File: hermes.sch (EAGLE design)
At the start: 13 parts

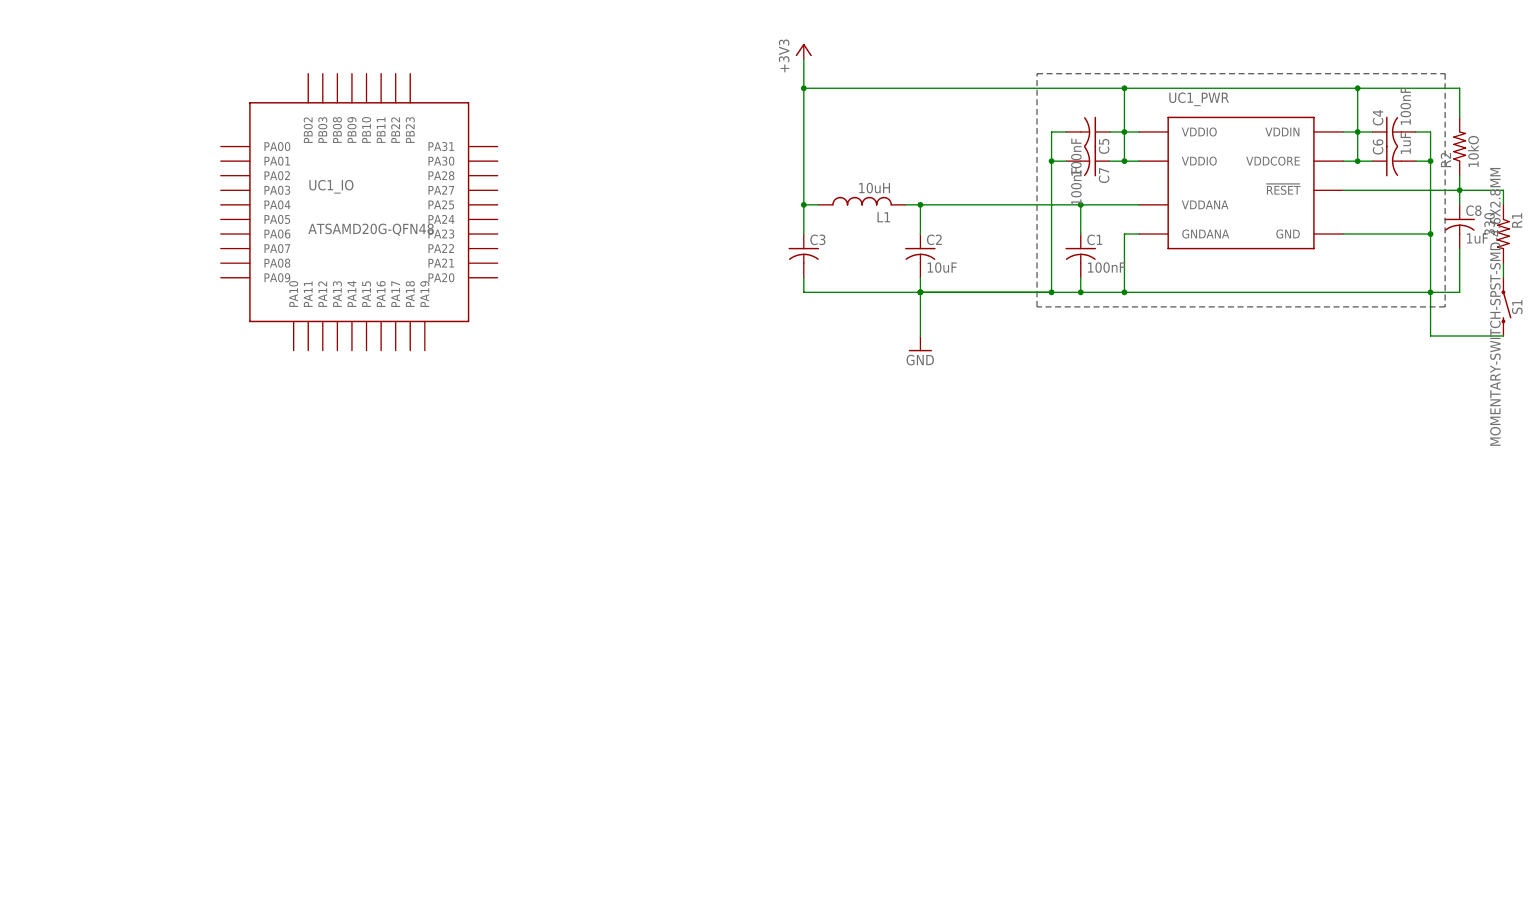
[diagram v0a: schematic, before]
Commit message: -Add LDO -Add library -Notes to uC PWR
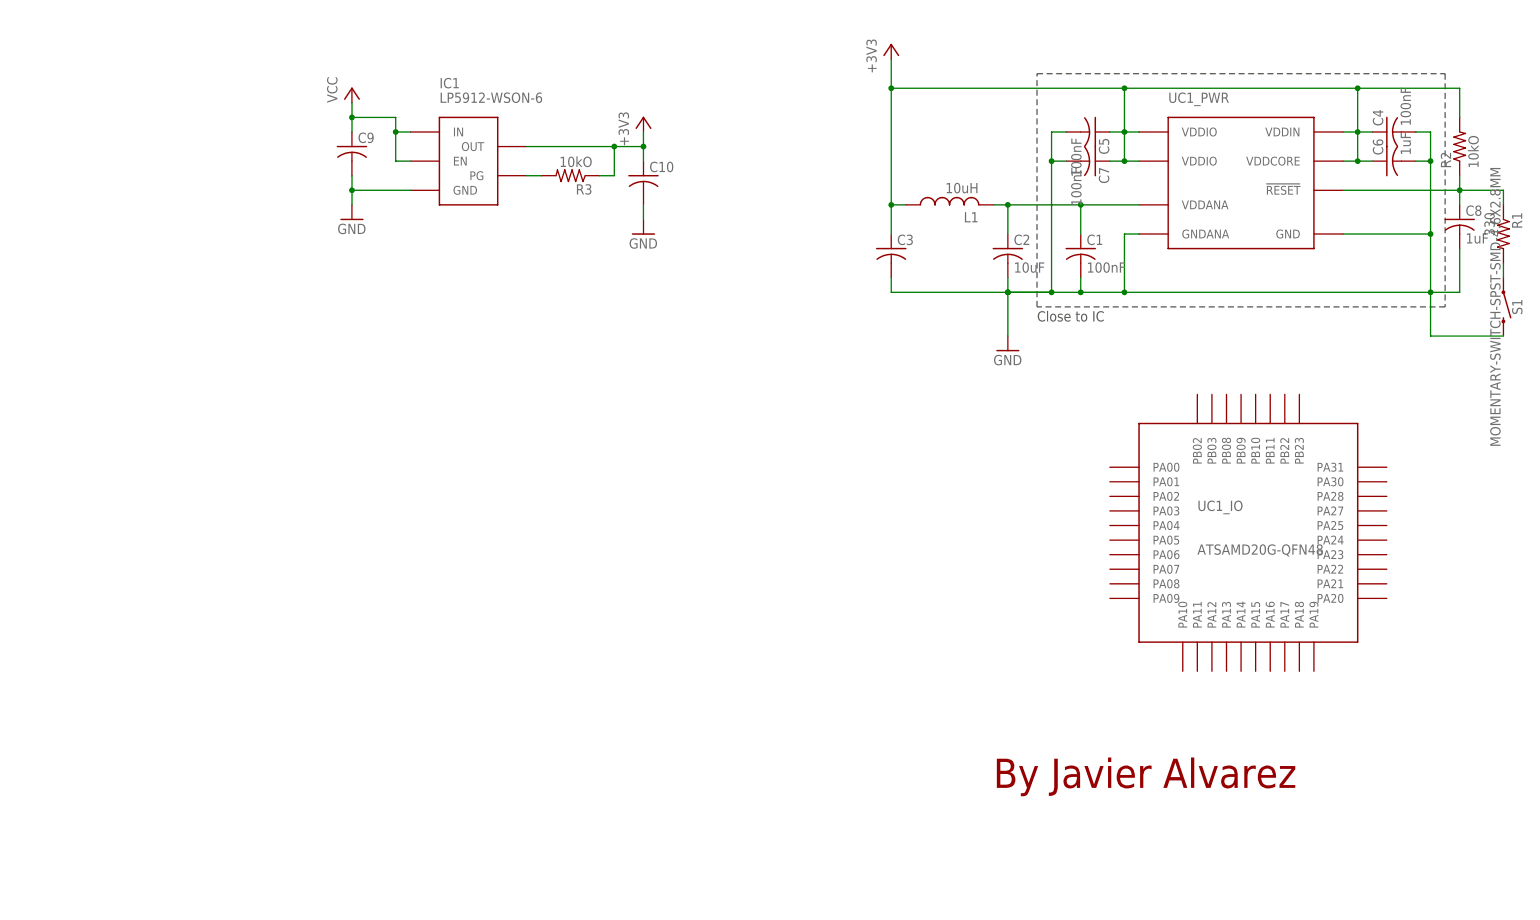
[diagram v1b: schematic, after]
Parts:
- added C10, C9: (no value), rcl:C-USC0201
- added IC1: LP5912-WSON-6, Hermes_lib:LP5912-WSON-6
- added R3: 10kO, rcl:R-US_R0201
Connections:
- new net N$4: IC1.PG, R3.2
- new net VCC: C9.1, IC1.EN, IC1.IN
- net +3V3: now also C10.1, IC1.OUT, R3.1
- net GND: now also C10.2, C9.2, IC1.GND
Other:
- note added: "By Javier Alvarez"
- note added: "Close to IC"
- moved on the sheet: C2, C3, L1, UC1_IO
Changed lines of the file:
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@@
 <part name="C8" library="rcl" library_urn="urn:adsk.eagle:library:334" deviceset="C-US" device="C0201" package3d_urn="urn:adsk.eagle:package:23690/1" value="1uF"/>
 <part name="S1" library="SparkFun-Switches" library_urn="urn:adsk.eagle:library:535" deviceset="MOMENTARY-SWITCH-SPST" device="-SMD-4.6X2.8MM" package3d_urn="urn:adsk.eagle:package:40176/1"/>
+<part name="IC1" library="Hermes_lib" library_urn="urn:adsk.eagle:library:1022648" deviceset="LP5912-" device="WSON-6" package3d_urn="urn:adsk.eagle:package:1286349/1"/>
+<part name="C9" library="rcl" library_urn="urn:adsk.eagle:library:334" deviceset="C-US" device="C0201" package3d_urn="urn:adsk.eagle:package:23690/1"/>
+<part name="R3" library="rcl" library_urn="urn:adsk.eagle:library:334" deviceset="R-US_" device="R0201" package3d_urn="urn:adsk.eagle:package:23593/1" value="10kO"/>
+<part name="C10" library="rcl" library_urn="urn:adsk.eagle:library:334" deviceset="C-US" device="C0201" package3d_urn="urn:adsk.eagle:package:23690/1"/>
+<part name="P+1" library="supply1" library_urn="urn:adsk.eagle:library:371" deviceset="VCC" device=""/>
+<part name="GND2" library="supply1" library_urn="urn:adsk.eagle:library:371" deviceset="GND" device=""/>
+<part name="GND3" library="supply1" library_urn="urn:adsk.eagle:library:371" deviceset="GND" device=""/>
+<part name="+3V2" library="supply1" library_urn="urn:adsk.eagle:library:371" deviceset="+3V3" device=""/>
 </parts>
 <sheets>
@@
 <wire x1="246.38" y1="111.76" x2="175.26" y2="111.76" width="0.1524" layer="97" style="shortdash"/>
 <wire x1="175.26" y1="111.76" x2="175.26" y2="152.4" width="0.1524" layer="97" style="shortdash"/>
+<text x="175.26" y="109.22" size="1.778" layer="97">Close to IC</text>
+<text x="167.64" y="27.94" size="5.08" layer="94">By Javier Alvarez</text>
 </plain>
 <instances>
 <instance part="FRAME1" gate="G$1" x="0" y="0"/>
 <instance part="FRAME1" gate="G$2" x="162.56" y="0"/>
-<instance part="UC1" gate="_IO" x="58.42" y="129.54"/>
+<instance part="UC1" gate="_IO" x="213.36" y="73.66"/>
 <instance part="UC1" gate="_PWR" x="210.82" y="134.62"/>
-<instance part="+3V1" gate="G$1" x="134.62" y="157.48"/>
-<instance part="GND1" gate="1" x="154.94" y="104.14"/>
-<instance part="L1" gate="G$1" x="144.78" y="129.54" rot="R90"/>
+<instance part="+3V1" gate="G$1" x="149.86" y="157.48"/>
+<instance part="GND1" gate="1" x="170.18" y="104.14"/>
+<instance part="L1" gate="G$1" x="160.02" y="129.54" rot="R90"/>
 <instance part="C1" gate="G$1" x="182.88" y="121.92"/>
-<instance part="C2" gate="G$1" x="154.94" y="121.92"/>
-<instance part="C3" gate="G$1" x="134.62" y="121.92"/>
+<instance part="C2" gate="G$1" x="170.18" y="121.92"/>
+<instance part="C3" gate="G$1" x="149.86" y="121.92"/>
 <instance part="C4" gate="G$1" x="236.22" y="142.24" rot="R90"/>
 <instance part="C5" gate="G$1" x="185.42" y="142.24" rot="R270"/>
@@
 <instance part="C8" gate="G$1" x="248.92" y="127"/>
 <instance part="S1" gate="G$1" x="256.54" y="111.76" rot="R270"/>
+<instance part="IC1" gate="G$1" x="73.66" y="134.62"/>
+<instance part="C9" gate="G$1" x="55.88" y="139.7"/>
+<instance part="R3" gate="G$1" x="93.98" y="134.62" rot="R180"/>
+<instance part="C10" gate="G$1" x="106.68" y="134.62"/>
+<instance part="P+1" gate="VCC" x="55.88" y="149.86"/>
+<instance part="GND2" gate="1" x="106.68" y="124.46"/>
+<instance part="GND3" gate="1" x="55.88" y="127"/>
+<instance part="+3V2" gate="G$1" x="106.68" y="144.78"/>
 </instances>
 <busses>
@@
 <wire x1="193.04" y1="129.54" x2="182.88" y2="129.54" width="0.1524" layer="91"/>
 <pinref part="C2" gate="G$1" pin="1"/>
-<wire x1="182.88" y1="129.54" x2="154.94" y2="129.54" width="0.1524" layer="91"/>
-<wire x1="154.94" y1="129.54" x2="152.4" y2="129.54" width="0.1524" layer="91"/>
-<wire x1="154.94" y1="124.46" x2="154.94" y2="129.54" width="0.1524" layer="91"/>
-<junction x="154.94" y="129.54"/>
+<wire x1="182.88" y1="129.54" x2="170.18" y2="129.54" width="0.1524" layer="91"/>
+<wire x1="170.18" y1="129.54" x2="167.64" y2="129.54" width="0.1524" layer="91"/>
+<wire x1="170.18" y1="124.46" x2="170.18" y2="129.54" width="0.1524" layer="91"/>
+<junction x="170.18" y="129.54"/>
 <pinref part="C1" gate="G$1" pin="1"/>
 <wire x1="182.88" y1="124.46" x2="182.88" y2="129.54" width="0.1524" layer="91"/>
@@
 <segment>
 <pinref part="+3V1" gate="G$1" pin="+3V3"/>
-<wire x1="134.62" y1="154.94" x2="134.62" y2="149.86" width="0.1524" layer="91"/>
+<wire x1="149.86" y1="154.94" x2="149.86" y2="149.86" width="0.1524" layer="91"/>
 <pinref part="L1" gate="G$1" pin="1"/>
-<wire x1="134.62" y1="149.86" x2="134.62" y2="129.54" width="0.1524" layer="91"/>
-<wire x1="134.62" y1="129.54" x2="137.16" y2="129.54" width="0.1524" layer="91"/>
+<wire x1="149.86" y1="149.86" x2="149.86" y2="129.54" width="0.1524" layer="91"/>
+<wire x1="149.86" y1="129.54" x2="152.4" y2="129.54" width="0.1524" layer="91"/>
 <pinref part="C3" gate="G$1" pin="1"/>
-<wire x1="134.62" y1="129.54" x2="134.62" y2="124.46" width="0.1524" layer="91"/>
-<junction x="134.62" y="129.54"/>
+<wire x1="149.86" y1="129.54" x2="149.86" y2="124.46" width="0.1524" layer="91"/>
+<junction x="149.86" y="129.54"/>
 <pinref part="UC1" gate="_PWR" pin="VDDIO@1"/>
 <pinref part="C7" gate="G$1" pin="1"/>
@@
 <junction x="190.5" y="142.24"/>
 <wire x1="190.5" y1="142.24" x2="190.5" y2="149.86" width="0.1524" layer="91"/>
-<wire x1="190.5" y1="149.86" x2="134.62" y2="149.86" width="0.1524" layer="91"/>
-<junction x="134.62" y="149.86"/>
+<wire x1="190.5" y1="149.86" x2="149.86" y2="149.86" width="0.1524" layer="91"/>
+<junction x="149.86" y="149.86"/>
 <pinref part="C6" gate="G$1" pin="1"/>
 <pinref part="UC1" gate="_PWR" pin="VDDCORE"/>
@@
 <junction x="231.14" y="149.86"/>
 </segment>
+<segment>
+<pinref part="IC1" gate="G$1" pin="OUT"/>
+<pinref part="C10" gate="G$1" pin="1"/>
+<wire x1="86.36" y1="139.7" x2="101.6" y2="139.7" width="0.1524" layer="91"/>
+<wire x1="101.6" y1="139.7" x2="106.68" y2="139.7" width="0.1524" layer="91"/>
+<wire x1="106.68" y1="139.7" x2="106.68" y2="137.16" width="0.1524" layer="91"/>
+<pinref part="R3" gate="G$1" pin="1"/>
+<wire x1="99.06" y1="134.62" x2="101.6" y2="134.62" width="0.1524" layer="91"/>
+<wire x1="101.6" y1="134.62" x2="101.6" y2="139.7" width="0.1524" layer="91"/>
+<junction x="101.6" y="139.7"/>
+<pinref part="+3V2" gate="G$1" pin="+3V3"/>
+<wire x1="106.68" y1="142.24" x2="106.68" y2="139.7" width="0.1524" layer="91"/>
+<junction x="106.68" y="139.7"/>
+</segment>
 </net>
 <net name="GND" class="0">
@@
 <pinref part="C2" gate="G$1" pin="2"/>
 <wire x1="182.88" y1="114.3" x2="177.8" y2="114.3" width="0.1524" layer="91"/>
-<wire x1="154.94" y1="114.3" x2="154.94" y2="116.84" width="0.1524" layer="91"/>
+<wire x1="170.18" y1="114.3" x2="170.18" y2="116.84" width="0.1524" layer="91"/>
 <pinref part="C1" gate="G$1" pin="2"/>
 <wire x1="182.88" y1="116.84" x2="182.88" y2="114.3" width="0.1524" layer="91"/>
 <junction x="182.88" y="114.3"/>
 <pinref part="C3" gate="G$1" pin="2"/>
-<wire x1="134.62" y1="116.84" x2="134.62" y2="114.3" width="0.1524" layer="91"/>
-<wire x1="134.62" y1="114.3" x2="177.8" y2="114.3" width="0.1524" layer="91"/>
-<junction x="154.94" y="114.3"/>
+<wire x1="149.86" y1="116.84" x2="149.86" y2="114.3" width="0.1524" layer="91"/>
+<wire x1="149.86" y1="114.3" x2="177.8" y2="114.3" width="0.1524" layer="91"/>
+<junction x="170.18" y="114.3"/>
 <pinref part="GND1" gate="1" pin="GND"/>
-<wire x1="177.8" y1="114.3" x2="154.94" y2="114.3" width="0.1524" layer="91"/>
-<wire x1="154.94" y1="106.68" x2="154.94" y2="114.3" width="0.1524" layer="91"/>
-<junction x="154.94" y="114.3"/>
+<wire x1="177.8" y1="114.3" x2="170.18" y2="114.3" width="0.1524" layer="91"/>
+<wire x1="170.18" y1="106.68" x2="170.18" y2="114.3" width="0.1524" layer="91"/>
+<junction x="170.18" y="114.3"/>
 <wire x1="190.5" y1="114.3" x2="243.84" y2="114.3" width="0.1524" layer="91"/>
 <wire x1="243.84" y1="114.3" x2="243.84" y2="124.46" width="0.1524" layer="91"/>
@@
 <wire x1="243.84" y1="106.68" x2="243.84" y2="114.3" width="0.1524" layer="91"/>
 </segment>
+<segment>
+<pinref part="C10" gate="G$1" pin="2"/>
+<pinref part="GND2" gate="1" pin="GND"/>
+<wire x1="106.68" y1="129.54" x2="106.68" y2="127" width="0.1524" layer="91"/>
+</segment>
+<segment>
+<pinref part="C9" gate="G$1" pin="2"/>
+<pinref part="GND3" gate="1" pin="GND"/>
+<wire x1="55.88" y1="134.62" x2="55.88" y2="132.08" width="0.1524" layer="91"/>
+<pinref part="IC1" gate="G$1" pin="GND"/>
+<wire x1="55.88" y1="132.08" x2="55.88" y2="129.54" width="0.1524" layer="91"/>
+<wire x1="66.04" y1="132.08" x2="55.88" y2="132.08" width="0.1524" layer="91"/>
+<junction x="55.88" y="132.08"/>
+</segment>
 </net>
 <net name="N$2" class="0">
@@
 </segment>
 </net>
+<net name="VCC" class="0">
+<segment>
+<pinref part="P+1" gate="VCC" pin="VCC"/>
+<pinref part="C9" gate="G$1" pin="1"/>
+<wire x1="55.88" y1="147.32" x2="55.88" y2="144.78" width="0.1524" layer="91"/>
+<pinref part="IC1" gate="G$1" pin="IN"/>
+<wire x1="55.88" y1="144.78" x2="55.88" y2="142.24" width="0.1524" layer="91"/>
+<wire x1="66.04" y1="142.24" x2="63.5" y2="142.24" width="0.1524" layer="91"/>
+<wire x1="63.5" y1="142.24" x2="63.5" y2="144.78" width="0.1524" layer="91"/>
+<wire x1="63.5" y1="144.78" x2="55.88" y2="144.78" width="0.1524" layer="91"/>
+<junction x="55.88" y="144.78"/>
+<wire x1="63.5" y1="142.24" x2="63.5" y2="137.16" width="0.1524" layer="91"/>
+<junction x="63.5" y="142.24"/>
+<pinref part="IC1" gate="G$1" pin="EN"/>
+<wire x1="63.5" y1="137.16" x2="66.04" y2="137.16" width="0.1524" layer="91"/>
+</segment>
+</net>
+<net name="N$4" class="0">
+<segment>
+<pinref part="R3" gate="G$1" pin="2"/>
+<pinref part="IC1" gate="G$1" pin="PG"/>
+<wire x1="88.9" y1="134.62" x2="86.36" y2="134.62" width="0.1524" layer="91"/>
+</segment>
+</net>
